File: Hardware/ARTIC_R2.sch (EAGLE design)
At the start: 96 parts, among them J1 U.FL, J2 THING_PLUS, Q1 20V/4.2A/52mΩ/1.4W, U1 32M SPI Flash, U2 1.8V/100mA, U3 ARTIC_R2, U4 RFPA0133, U5 AS179-92LF, U6 DUAL-OPTOISOLATOR_SOIC8, X1 CRYSTAL-TCXO-26MHZ

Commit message: Nearing completion
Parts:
- added D3: RED, SparkFun-LED:LED-RED0603
- added JP5: JUMPER-SMT_2_NC_TRACE_SILK, SparkFun-Jumpers:JUMPER-SMT_2_NC_TRACE_SILK
- added R15: 1k, SparkFun-Resistors:1KOHM-0402T-1/16W-1%
- added SPARKX1, SPARKX2: SPARKX-LOGO4, SparkX:SPARKX-LOGO4
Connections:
- new net N$37: D3.A, R15.1
- new net N$38: D3.C, JP5.2
- net BOOT: now also J2.GPIO4
- net G16: now also J2.GPIO5
- net G8: now also J2.GPIO6
- net GND: now also JP5.1
- net INT1: now also J2.GPIO3
- net INT2: now also J2.GPIO2
- net PWR_EN: now also J2.GPIO0
- net RESETB: now also J2.GPIO1
- net VDD: now also R15.2
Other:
- note added: "LED"
- moved on the sheet: C2, C45, L1, R11, R2, U1

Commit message: Adjusted the RF track widths
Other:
- note added: "RF Track Impedance: Coplanar Waveguide with Ground Calculations ---------------- TX: 400MHz Ground is on layer 2. Prepreg thickness: 0.140mm 10 mil track with 5 mil gap = 49.8 Ohms Er = 4.3 ---------------- RX: 466MHz Ground is on layer 15 (there is a cut-out on layer 2 as per AnSem's design guide). Prepreg + layer 2 + core thickness = 1.375mm 24 mil track with 3 mil gap = 49.9 Ohms Er = 4.3"
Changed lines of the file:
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@@
 <text x="391.16" y="213.36" size="5.08" layer="97">Antenna</text>
 <text x="167.64" y="30.48" size="5.08" layer="97">ARTIC R2</text>
-<text x="322.58" y="73.66" size="5.08" layer="97">RF Amp</text>
+<text x="327.66" y="81.28" size="5.08" layer="97">RF Amp</text>
 <text x="43.18" y="12.7" size="5.08" layer="97">Pins</text>
 <text x="256.032" y="89.662" size="1.27" layer="97">50Ω</text>
@@
 <wire x1="127" y1="205.74" x2="127" y2="279.4" width="0.2032" layer="97" style="longdash"/>
 <text x="107.442" y="213.614" size="5.08" layer="97">LED</text>
+<text x="330.962" y="69.088" size="1.778" layer="97" font="vector" align="top-left">RF Track Impedance: Coplanar Waveguide with Ground Calculations
+----------------
+TX: 400MHz
+Ground is on layer 2. Prepreg thickness: 0.140mm
+10 mil track with 5 mil gap = 49.8 Ohms
+Er = 4.3
+----------------
+RX: 466MHz
+Ground is on layer 15 (there is a cut-out on layer 2 as per AnSem's design guide).
+Prepreg + layer 2 + core thickness = 1.375mm
+24 mil track with 3 mil gap = 49.9 Ohms
+Er = 4.3
+</text>
 </plain>
 <instances>
@@
 </segment>
 <segment>
-<wire x1="60.96" y1="53.34" x2="63.5" y2="53.34" width="0.1524" layer="91"/>
 <label x="63.5" y="53.34" size="1.27" layer="95" xref="yes"/>
 <pinref part="J2" gate="G$1" pin="A5"/>
-<wire x1="60.96" y1="53.34" x2="63.5" y2="53.34" width="0.1524" layer="91"/>
 <wire x1="63.5" y1="53.34" x2="60.96" y2="53.34" width="0.1524" layer="91"/>
 </segment>

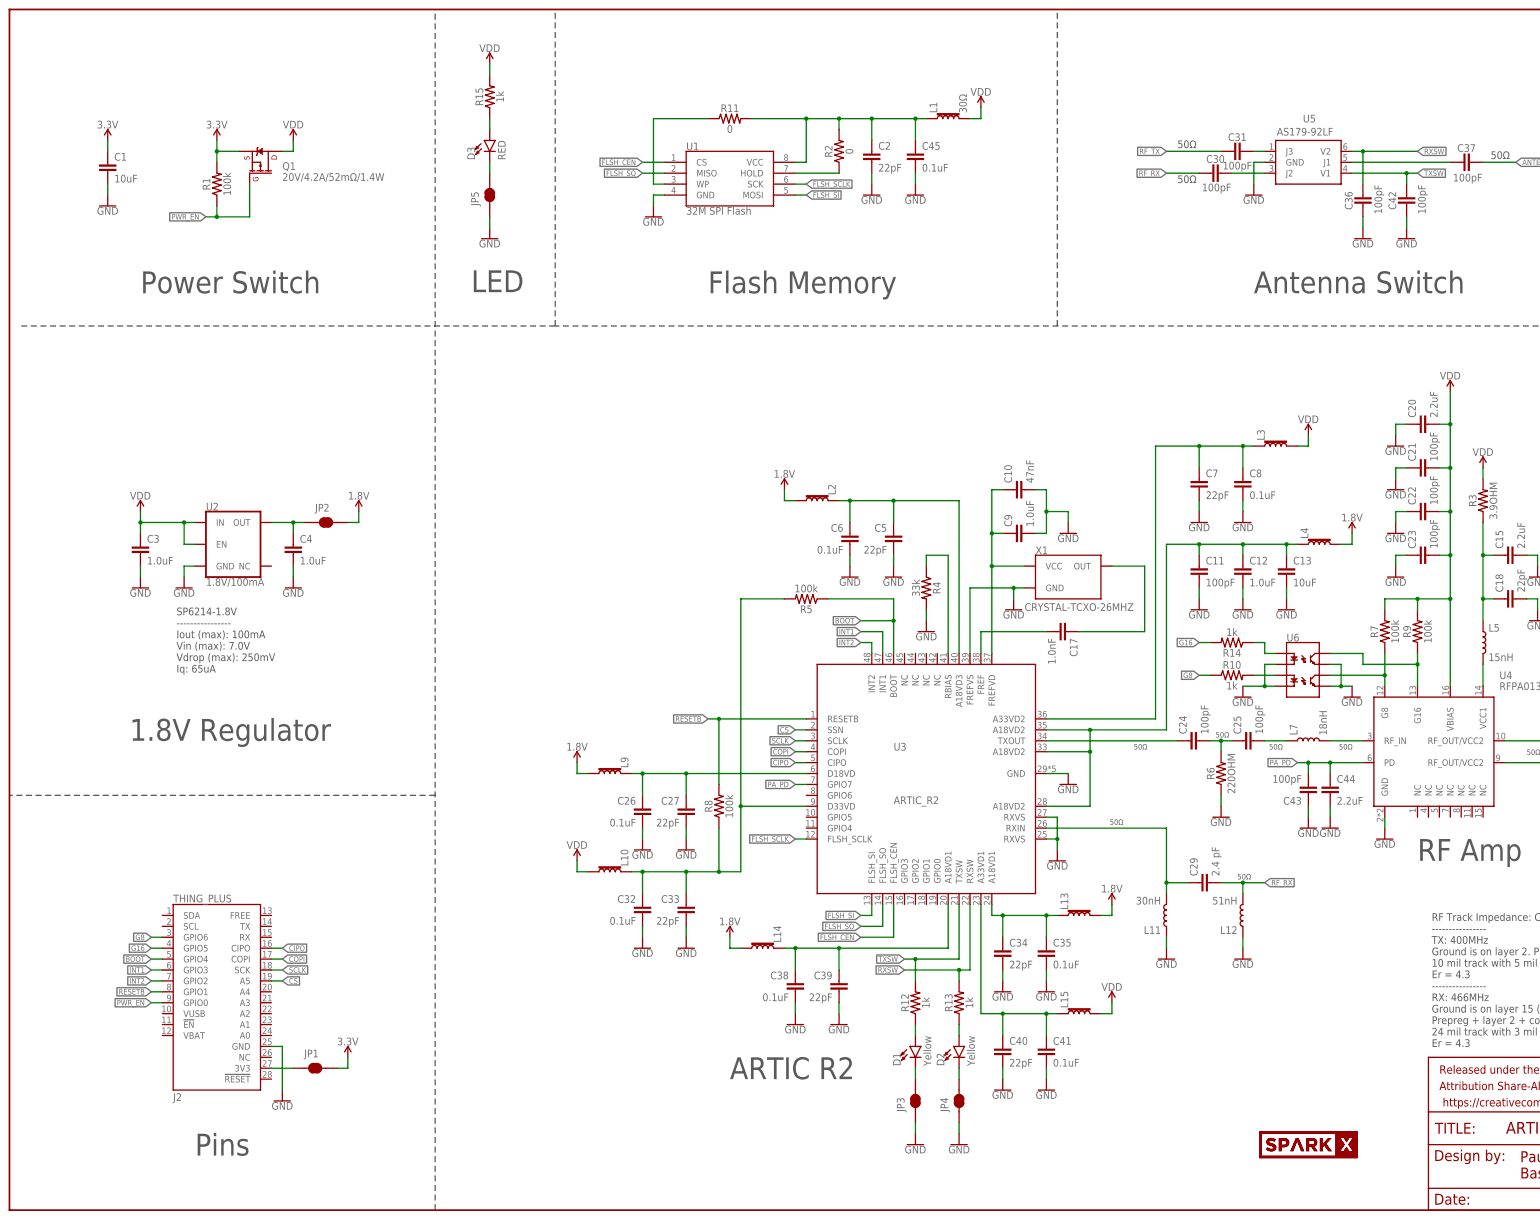
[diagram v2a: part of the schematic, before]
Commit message: Added 4x4 test panel
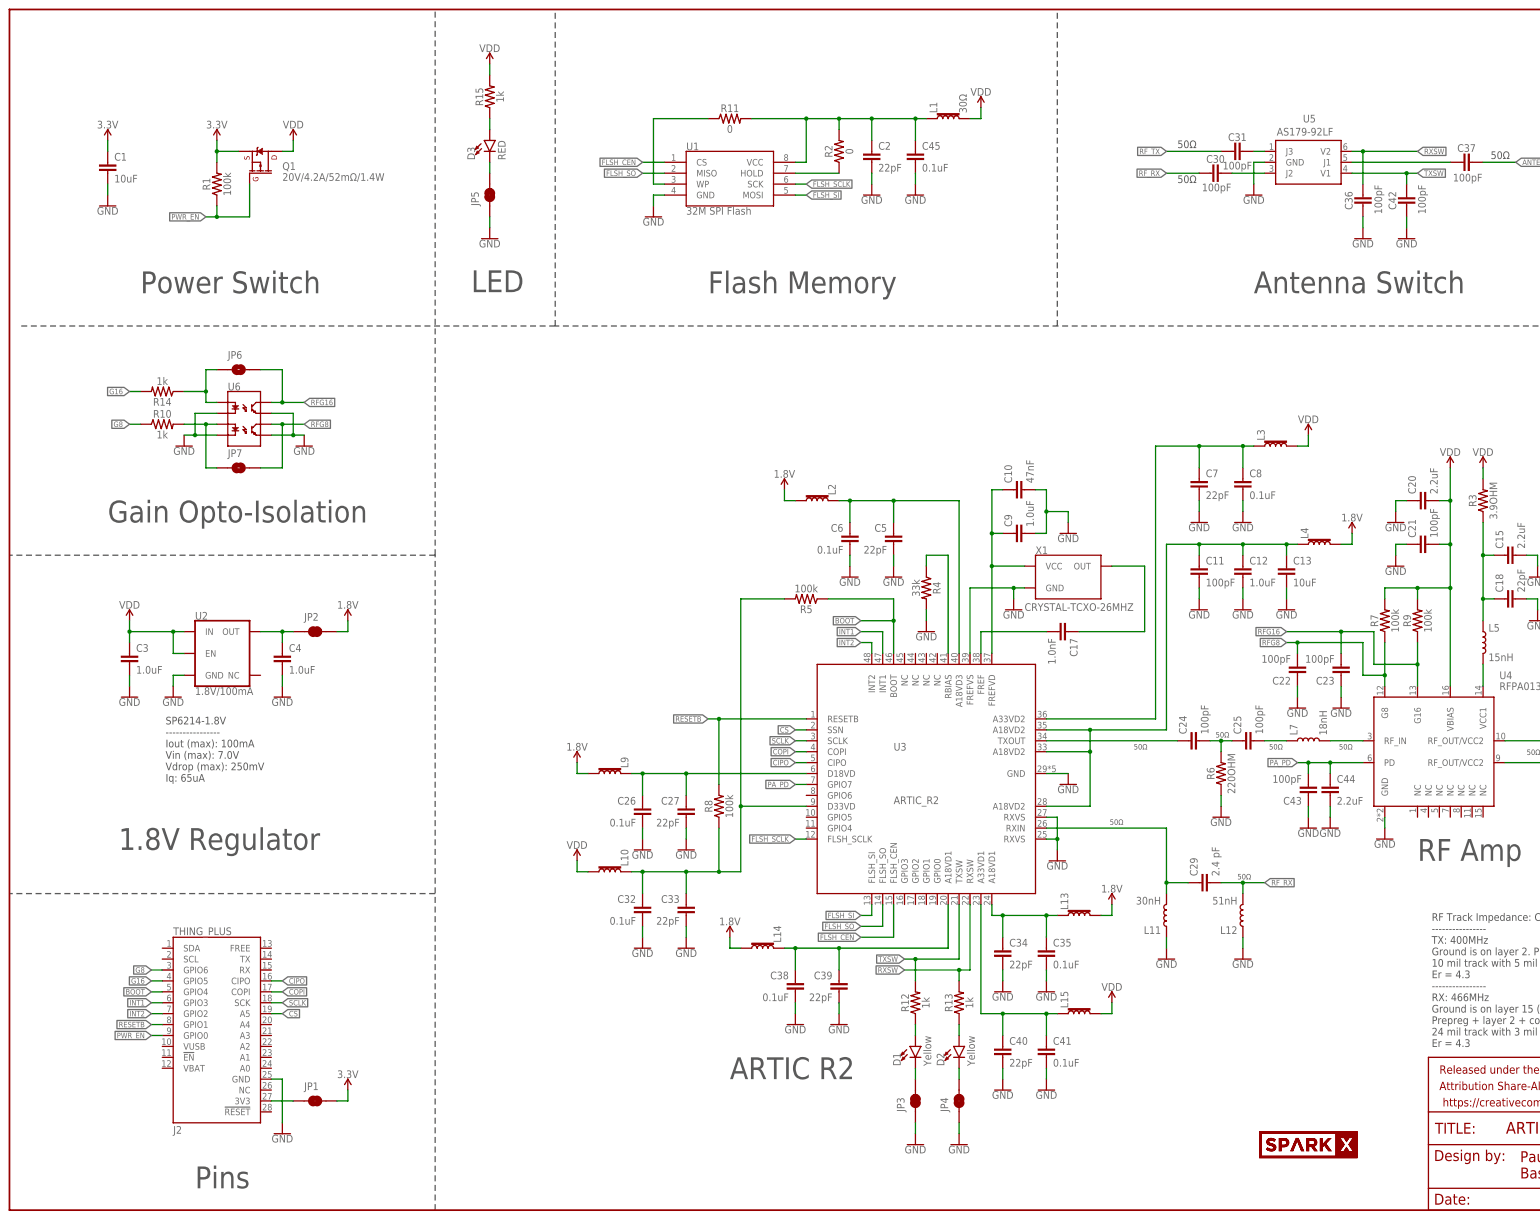
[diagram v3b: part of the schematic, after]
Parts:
- added JP6, JP7: JUMPER-SMT_2_NO_SILK, SparkFun-Jumpers:JUMPER-SMT_2_NO_SILK
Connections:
- removed net N$33: R9.1, U4.G16, U6.CL1
- removed net N$34: R7.1, U4.G8, U6.CL2
- new net RFG16: C23.2, JP6.2, R9.1, U4.G16, U6.CL1
- new net RFG8: C22.2, JP7.2, R7.1, U4.G8, U6.CL2
- net N$23: now also JP7.1
- net N$27: now also JP6.1
- net VDD: no longer C22.2, C23.2
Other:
- note added: "Gain Opto-Isolation"
- moved on the sheet: C20, C21, C22, C23, C3, C4, J2, JP1, JP2, R10, R14, R7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

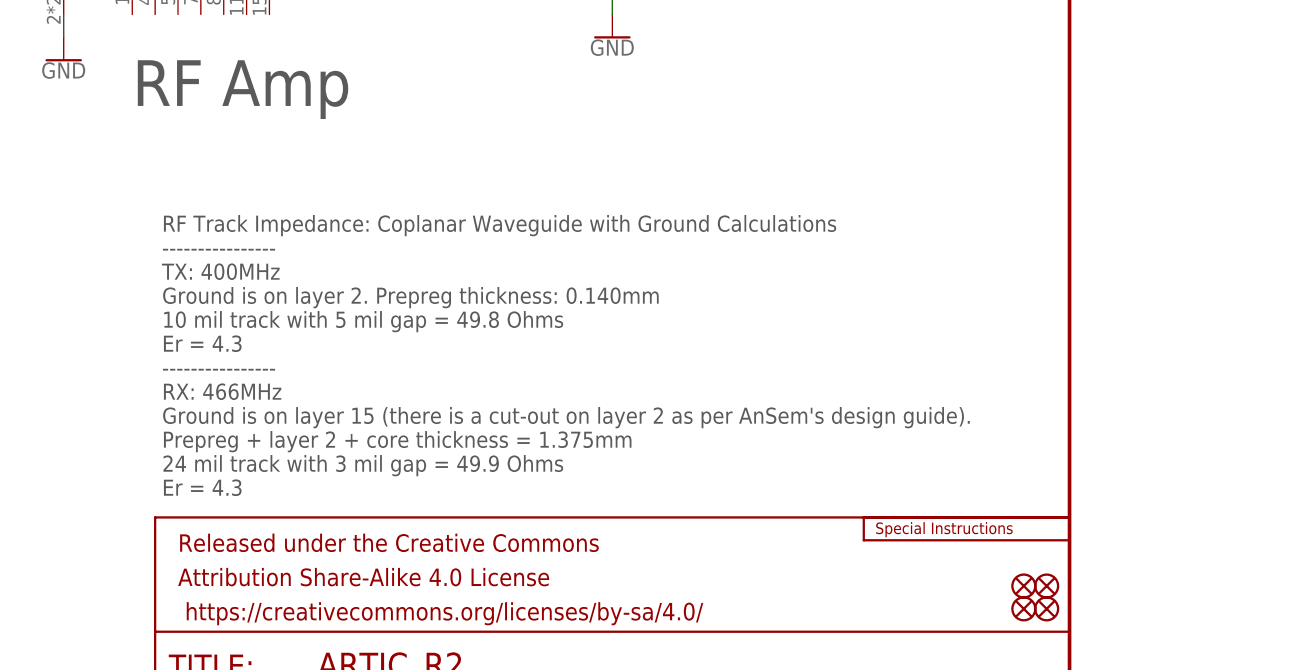
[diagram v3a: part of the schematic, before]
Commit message: ).8mm PCB with Impedance Control
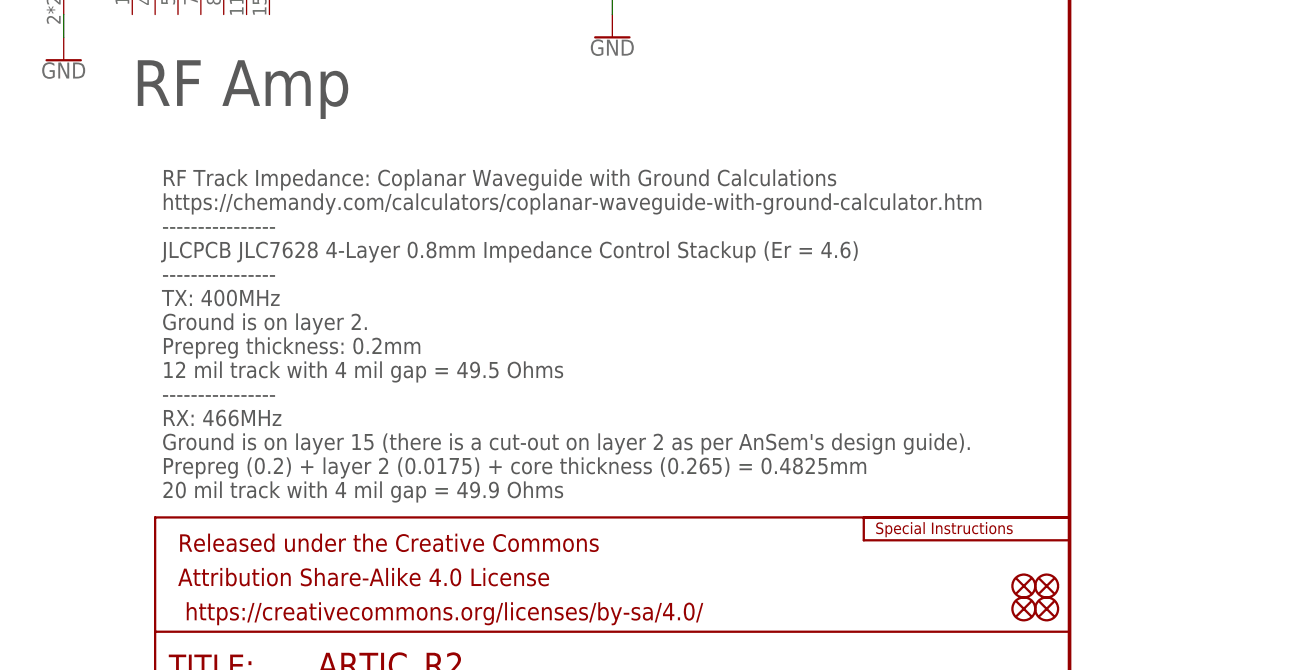
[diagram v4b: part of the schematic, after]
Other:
- note added: "RF Track Impedance: Coplanar Waveguide with Ground Calculations https://chemandy.com/calculators/coplanar-waveguide-with-ground-calculator.htm ---------------- JLCPCB JLC7628 4-Layer 0.8mm Impedance Control Stackup (Er = 4.6) ---------------- TX: 400MHz Ground is on layer 2. Prepreg thickness: 0.2mm 12 mil track with 4 mil gap = 49.5 Ohms ---------------- RX: 466MHz Ground is on layer 15 (there i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"
- note removed: "RF Track Impedance: Coplanar Waveguide with Ground Calculations ---------------- TX: 400MHz Ground is on layer 2. Prepreg thickness: 0.140mm 10 mil track with 5 mil gap = 49.8 Ohms Er = 4.3 ---------------- RX: 466MHz Ground is on layer 15 (there is a cut-out on layer 2 as per AnSem's design guide). Prepreg + layer 2 + core thickness = 1.375mm 24 mil track with 3 mil gap = 49.9 Ohms Er = 4.3"
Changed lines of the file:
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@@
 <wire x1="127" y1="205.74" x2="127" y2="279.4" width="0.2032" layer="97" style="longdash"/>
 <text x="107.442" y="213.614" size="5.08" layer="97">LED</text>
-<text x="330.962" y="69.088" size="1.778" layer="97" font="vector" align="top-left">RF Track Impedance: Coplanar Waveguide with Ground Calculations
+<text x="330.962" y="74.168" size="1.778" layer="97" font="vector" align="top-left">RF Track Impedance: Coplanar Waveguide with Ground Calculations
+https://chemandy.com/calculators/coplanar-waveguide-with-ground-calculator.htm
+----------------
+JLCPCB JLC7628 4-Layer 0.8mm Impedance Control Stackup (Er = 4.6)
 ----------------
 TX: 400MHz
-Ground is on layer 2. Prepreg thickness: 0.140mm
-10 mil track with 5 mil gap = 49.8 Ohms
-Er = 4.3
+Ground is on layer 2.
+Prepreg thickness: 0.2mm
+12 mil track with 4 mil gap = 49.5 Ohms
 ----------------
 RX: 466MHz
 Ground is on layer 15 (there is a cut-out on layer 2 as per AnSem's design guide).
-Prepreg + layer 2 + core thickness = 1.375mm
-24 mil track with 3 mil gap = 49.9 Ohms
-Er = 4.3
+Prepreg (0.2) + layer 2 (0.0175) + core thickness (0.265) = 0.4825mm
+20 mil track with 4 mil gap = 49.9 Ohms
 </text>
 <wire x1="99.06" y1="152.4" x2="0" y2="152.4" width="0.2032" layer="97" style="longdash"/>
